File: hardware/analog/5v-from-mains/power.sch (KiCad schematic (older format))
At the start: 13 parts, among them J1 Conn_WallSocket_Earth, J2 Conn_WallSocket_Earth, U7 LM7805_TO220

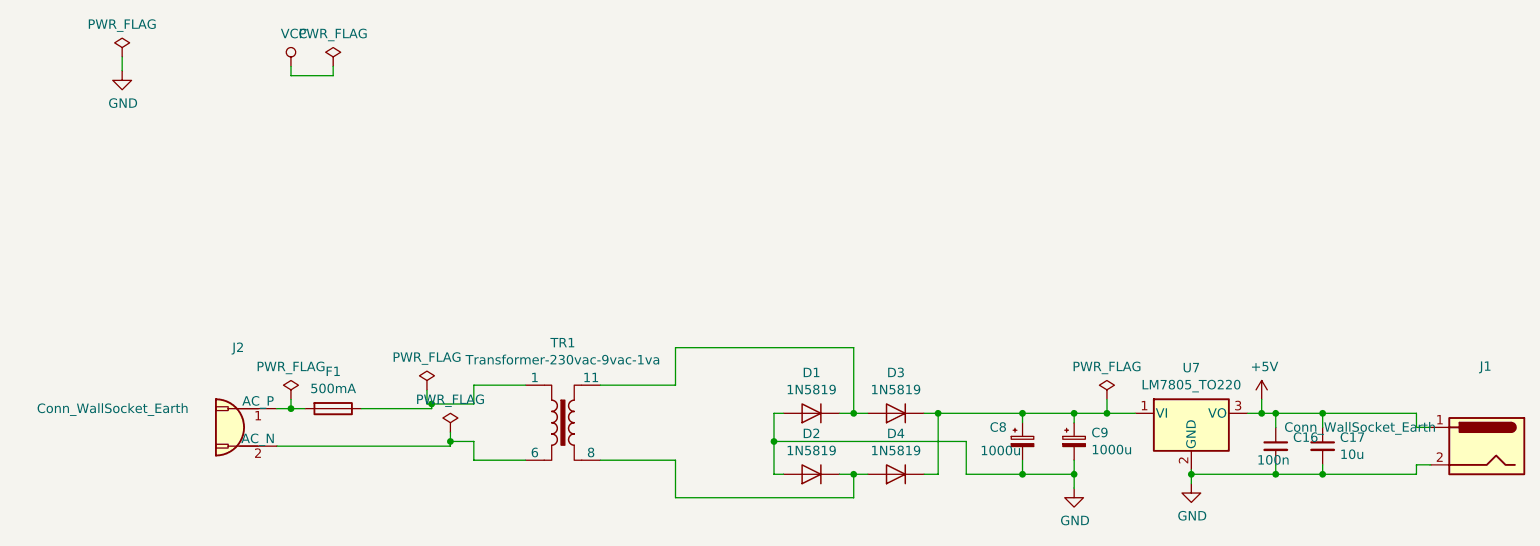
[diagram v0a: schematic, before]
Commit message: Added voltage reference REF5020 datasheet
Started work on HW rev 2 of electro load and 5v-from-mains - rev 1 contained misaligned footprints.
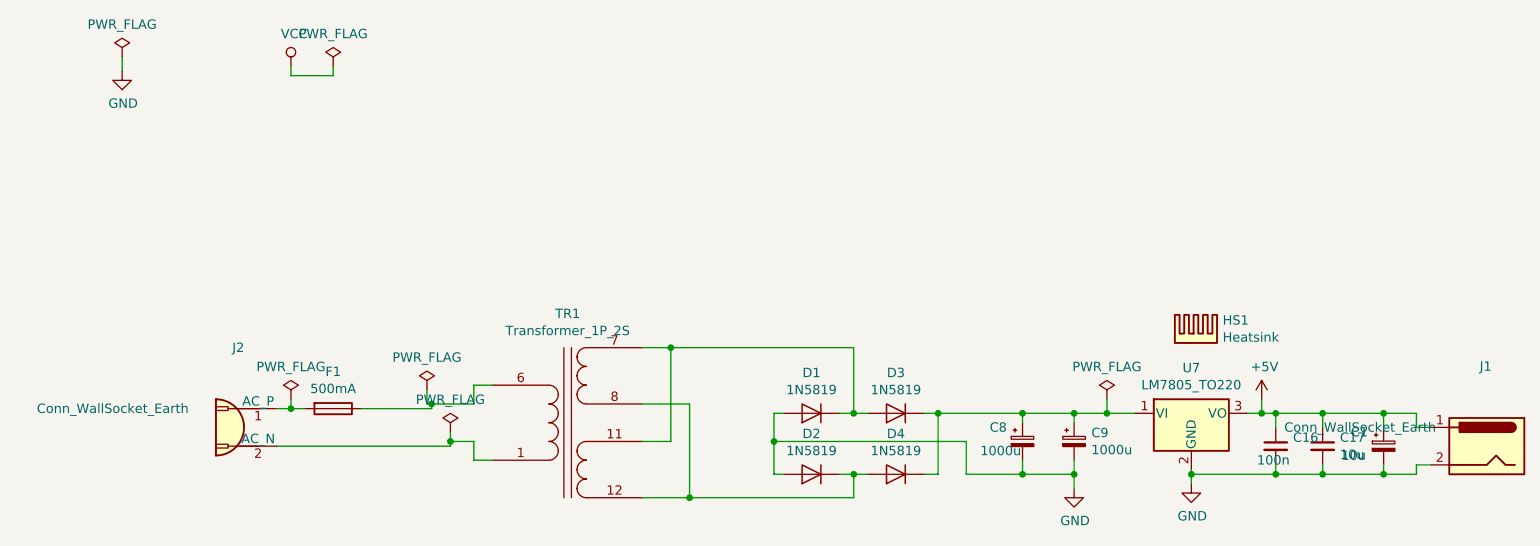
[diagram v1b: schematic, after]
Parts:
- removed TR1: Transformer-230vac-9vac-1va, Transformer_THT:Transformer_Breve_TEZ-44x52, symbol athir:Transformer-230vac-9vac-1va
- added C1: 10u, Capacitor_THT:CP_Radial_D6.3mm_P2.50mm, symbol Device:CP_Small
- added HS1: Heatsink, athir:Heatsink_Fischer_SK104-STC-STIC_35x13mm_2xDrill2.5mm, symbol Mechanical:Heatsink
- added TR1: Transformer_1P_2S, Transformer_THT:Transformer_Breve_TEZ-44x52, symbol athir:Transformer_1P_2S
- F1: footprint Fuse:Fuseholder_Cylinder-5x20mm_Schurter_0031_8201_Horizontal_Open -> athir:KK-Fuseholder
- J1, J2: footprint athir:230VAC_PLUG -> athir:Molex-KK-396-5277
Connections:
- net +5V: now also C1.1
- net GND: now also C1.2
- net at J2.2 (AC_N): now also TR1.1 (AB)
- net at D1.1 (K), D3.2 (A): now also TR1.11 (SC), TR1.7 (SA)
- net at D2.1 (K), D4.2 (A): now also TR1.12 (SD), TR1.8 (SB)
- net at F1.1: now also TR1.6 (AA)
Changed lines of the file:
@@
 F 0 "J1" H 9431 5225 50  0000 C CNN
 F 1 "Conn_WallSocket_Earth" H 10100 4900 50  0000 C CNN
-F 2 "athir:230VAC_PLUG" H 9125 4900 50  0001 C CNN
+F 2 "athir:Molex-KK-396-5277" H 9125 4900 50  0001 C CNN
 F 3 "" H 9125 4900 50  0001 C CNN
 	1    9425 4800
@@
 $EndComp
 Wire Wire Line
-	5100 4475 4700 4475
-Wire Wire Line
-	5100 4275 5100 4475
-Wire Wire Line
-	8550 4950 9050 4950
+	8550 4950 8875 4950
 Connection ~ 8550 4950
 Wire Wire Line
 	8550 4900 8550 4950
 Wire Wire Line
-	9050 4625 8550 4625
+	9050 4625 8875 4625
 Connection ~ 8550 4625
 Wire Wire Line
@@
 F 0 "F1" V 3078 4600 50  0000 C CNN
 F 1 "500mA" V 3169 4600 50  0000 C CNN
-F 2 "Fuse:Fuseholder_Cylinder-5x20mm_Schurter_0031_8201_Horizontal_Open" V 3205 4600 50  0001 C CNN
+F 2 "athir:KK-Fuseholder" V 3205 4600 50  0001 C CNN
 F 3 "~" H 3275 4600 50  0001 C CNN
 	1    3275 4600
@@
 	4025 4875 4025 4775
 Wire Wire Line
-	4300 4875 4025 4875
-Wire Wire Line
-	4025 4475 4300 4475
-Wire Wire Line
 	4025 4575 4025 4475
 $Comp
@@
 F 0 "J2" H 2781 5125 50  0000 C CNN
 F 1 "Conn_WallSocket_Earth" H 3450 4800 50  0000 C CNN
-F 2 "athir:230VAC_PLUG" H 2475 4800 50  0001 C CNN
+F 2 "athir:Molex-KK-396-5277" H 2475 4800 50  0001 C CNN
 F 3 "" H 2475 4800 50  0001 C CNN
 	1    2775 4700
@@
 	7400 4625 7225 4625
 Wire Wire Line
-	5100 4275 6050 4275
-Wire Wire Line
-	5100 5075 6050 5075
-Wire Wire Line
-	5100 5075 5100 4875
-Wire Wire Line
-	5100 4875 4700 4875
-$Comp
-L athir:Transformer-230vac-9vac-1va TR1
-U 1 1 5E860CD2
-P 4500 4675
-F 0 "TR1" H 4500 5100 50  0000 C CNN
-F 1 "Transformer-230vac-9vac-1va" H 4500 5009 50  0000 C CNN
-F 2 "Transformer_THT:Transformer_Breve_TEZ-44x52" H 4500 4675 50  0001 C CNN
-F 3 "" H 4500 4675 50  0001 C CNN
-	1    4500 4675
-	1    0    0    -1
-$EndComp
+	5075 4275 6050 4275
 $Comp
 L Device:CP_Small C?
@@
 	1    0    0    -1
 $EndComp
+$Comp
+L Mechanical:Heatsink HS1
+U 1 1 5E968A90
+P 7875 4250
+F 0 "HS1" H 8017 4371 50  0000 L CNN
+F 1 "Heatsink" H 8017 4280 50  0000 L CNN
+F 2 "athir:Heatsink_Fischer_SK104-STC-STIC_35x13mm_2xDrill2.5mm" H 7887 4250 50  0001 C CNN
+F 3 "~" H 7887 4250 50  0001 C CNN
+	1    7875 4250
+	1    0    0    -1
+$EndComp
+$Comp
+L Device:CP_Small C?
+U 1 1 5E96F498
+P 8875 4800
+AR Path="/5E96F498" Ref="C?"  Part="1"
+AR Path="/5E8D69C1/5E96F498" Ref="C1"  Part="1"
+F 0 "C1" H 8700 4875 50  0000 L CNN
+F 1 "10u" H 8650 4750 50  0000 L CNN
+F 2 "Capacitor_THT:CP_Radial_D6.3mm_P2.50mm" H 8875 4800 50  0001 C CNN
+F 3 "~" H 8875 4800 50  0001 C CNN
+	1    8875 4800
+	1    0    0    -1
+$EndComp
+Wire Wire Line
+	8875 4700 8875 4625
+Connection ~ 8875 4625
+Wire Wire Line
+	8875 4625 8550 4625
+Connection ~ 8875 4950
+Wire Wire Line
+	8875 4950 9050 4950
+Wire Wire Line
+	8875 4900 8875 4950
+$Comp
+L athir:Transformer_1P_2S TR1
+U 1 1 5E98CD1A
+P 4525 4675
+F 0 "TR1" H 4525 5256 50  0000 C CNN
+F 1 "Transformer_1P_2S" H 4525 5165 50  0000 C CNN
+F 2 "Transformer_THT:Transformer_Breve_TEZ-44x52" H 4525 4675 50  0001 C CNN
+F 3 "~" H 4525 4675 50  0001 C CNN
+	1    4525 4675
+	1    0    0    -1
+$EndComp
+Wire Wire Line
+	4125 4475 4025 4475
+Wire Wire Line
+	4025 4875 4125 4875
+Wire Wire Line
+	4925 4775 5075 4775
+Wire Wire Line
+	5075 4275 5075 4775
+Wire Wire Line
+	5075 4275 4925 4275
+Connection ~ 5075 4275
+Wire Wire Line
+	4925 4575 5175 4575
+Wire Wire Line
+	5175 4575 5175 5075
+Connection ~ 5175 5075
+Wire Wire Line
+	5175 5075 6050 5075
+Wire Wire Line
+	4925 5075 5175 5075
 $EndSCHEMATC
